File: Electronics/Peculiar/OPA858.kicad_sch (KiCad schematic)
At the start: 12 parts, among them U12 ${SIM.PARAMS}, U13 ${SIM.PARAMS}

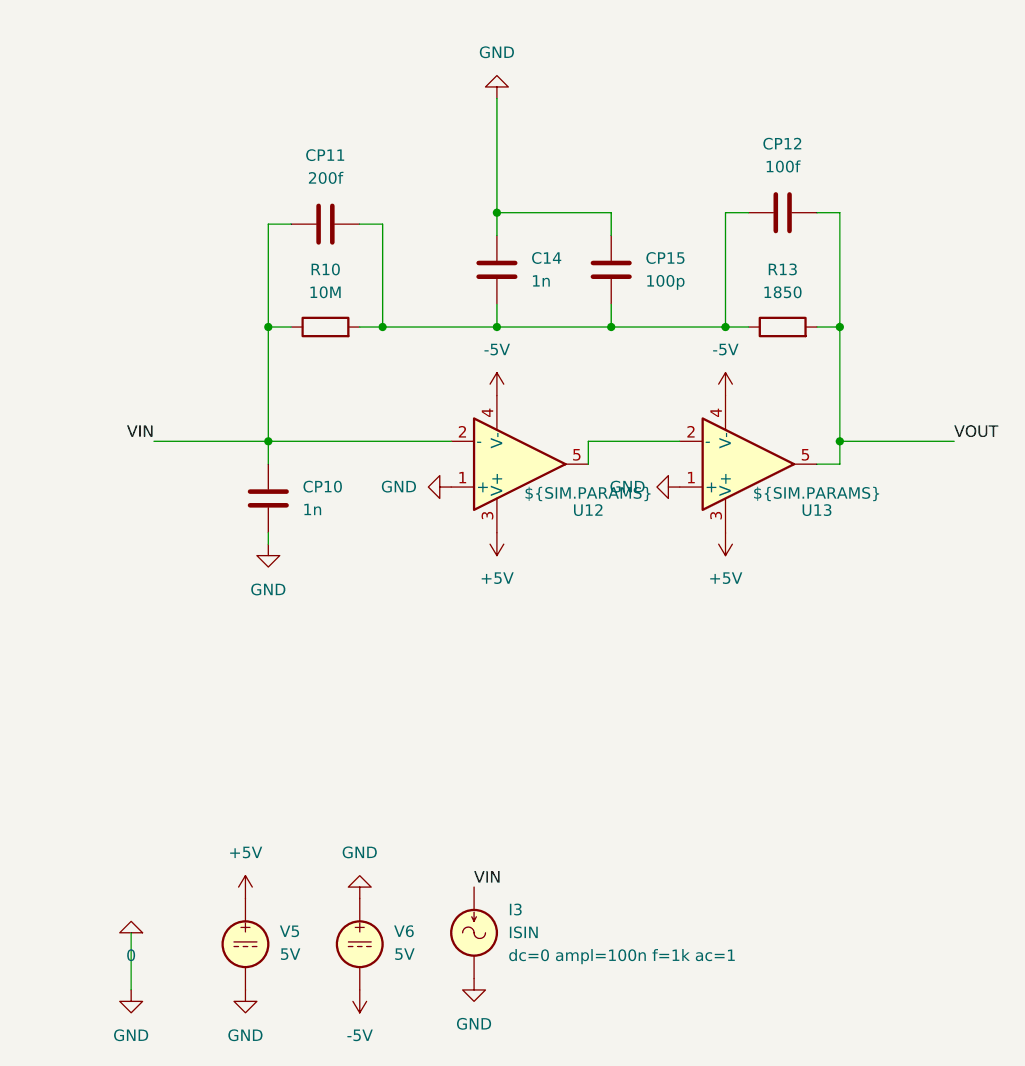
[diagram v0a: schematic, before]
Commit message: Improve the peculiar TIA
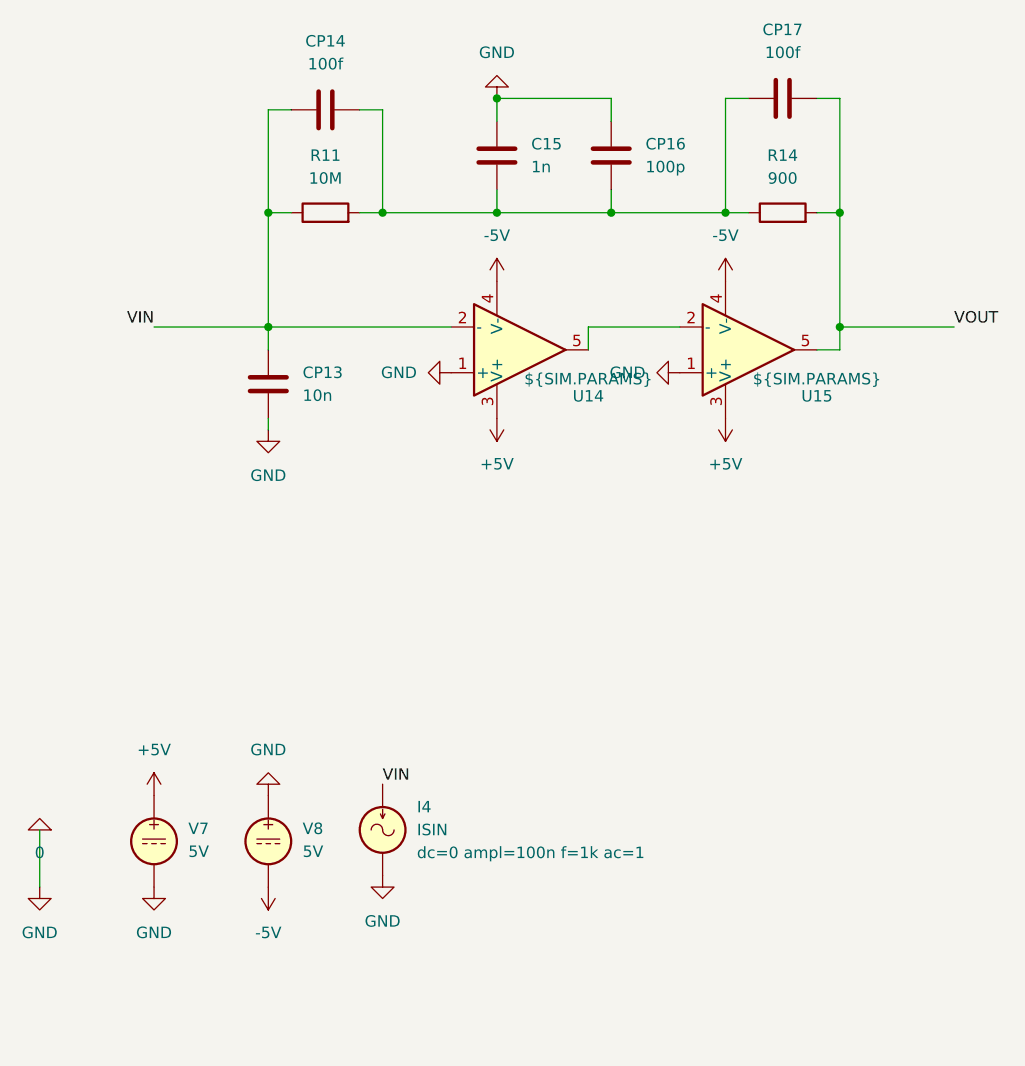
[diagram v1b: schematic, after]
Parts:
- removed C14, CP10: 1n, symbol Device:C
- removed CP11: 200f, symbol Device:C
- removed CP12: 100f, symbol Device:C
- removed CP15: 100p, symbol Device:C
- removed I3: ISIN, symbol Simulation_SPICE:ISIN
- removed R10: 10M, symbol Device:R
- removed R13: 1850, symbol Device:R
- removed U12, U13: ${SIM.PARAMS}, symbol Simulation_SPICE:OPAMP
- removed V5, V6: 5V, symbol Simulation_SPICE:VDC
- added C15: 1n, symbol Device:C
- added CP13: 10n, symbol Device:C
- added CP14, CP17: 100f, symbol Device:C
- added CP16: 100p, symbol Device:C
- added I4: ISIN, symbol Simulation_SPICE:ISIN
- added R11: 10M, symbol Device:R
- added R14: 900, symbol Device:R
- added U14, U15: ${SIM.PARAMS}, symbol Simulation_SPICE:OPAMP
- added V7, V8: 5V, symbol Simulation_SPICE:VDC
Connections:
- net +5V: now also U14.3 (V+), U15.3 (V+), V7.1
- net -5V: now also U14.4 (V-), U15.4 (V-), V8.2
- net 0: now also C15.2, CP13.2, CP16.2, I4.2, U14.1 (+), U15.1 (+), V7.2, V8.1
- net VIN: now also CP13.1, CP14.1, I4.1, R11.1, U14.2 (-)
- net VOUT: now also CP17.2, R14.2, U15.5
- new net: C15.1, CP14.2, CP16.1, CP17.1, R11.2, R14.1
- new net: U14.5, U15.2 (-)
